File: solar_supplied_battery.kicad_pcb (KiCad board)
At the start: 2 copper layers, 16 parts, among them J1 Conn_01x02_Pin, J2 Conn_01x02_Pin, J3 Conn_01x02_Pin, J4 Conn_01x02_Pin, Q1 2N7002, U1 AP3015AKTR-G1

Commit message: starting routes
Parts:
- J1, J2: footprint Connector_PinHeader_2.54mm:PinHeader_1x02_P2.54mm_Vertical -> TerminalBlock:TerminalBlock_MaiXu_MX126-5.0-02P_1x02_P5.00mm
- J4: footprint Connector_PinHeader_2.54mm:PinHeader_1x02_P2.54mm_Horizontal -> TerminalBlock:TerminalBlock_MaiXu_MX126-5.0-02P_1x02_P5.00mm
- moved J1 90.3 mm to (105.1, 68.0), turned to 90 degrees
- moved R4 80.1 mm to (91.2, 61.2), turned to 180 degrees
- moved C2 79.5 mm to (99.0, 68.0), turned to 90 degrees
- moved C3 77.0 mm to (98.3, 61.2), turned to 180 degrees
- moved R3 75.3 mm to (87.6, 66.9)
- moved C1 72.0 mm to (90.3, 69.1), turned to 90 degrees
- moved R2 68.4 mm to (94.6, 65.4), turned to 180 degrees
- moved R1 65.3 mm to (98.4, 63.9), turned to 180 degrees
- moved Q1 55.3 mm to (91.2, 64.8), turned to -90 degrees
- moved U1 50.8 mm to (94.4, 69.2), turned to 180 degrees
- moved L1 47.4 mm to (89.8, 75.1), turned to 180 degrees
- moved J4 45.6 mm to (78.0, 62.0)
- moved J2 41.9 mm to (75.4, 73.1), turned to 180 degrees
- moved J3 38.5 mm to (82.3, 74.4), turned to 180 degrees
- moved D2 35.8 mm to (84.0, 65.5), turned to 90 degrees
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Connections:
- D1 pad A: /OUT_P -> Net-(U1-SW)
- L1 pad 1: /OUT_P -> Net-(U1-SW)
- U1 pad 1: /OUT_P -> Net-(U1-SW)

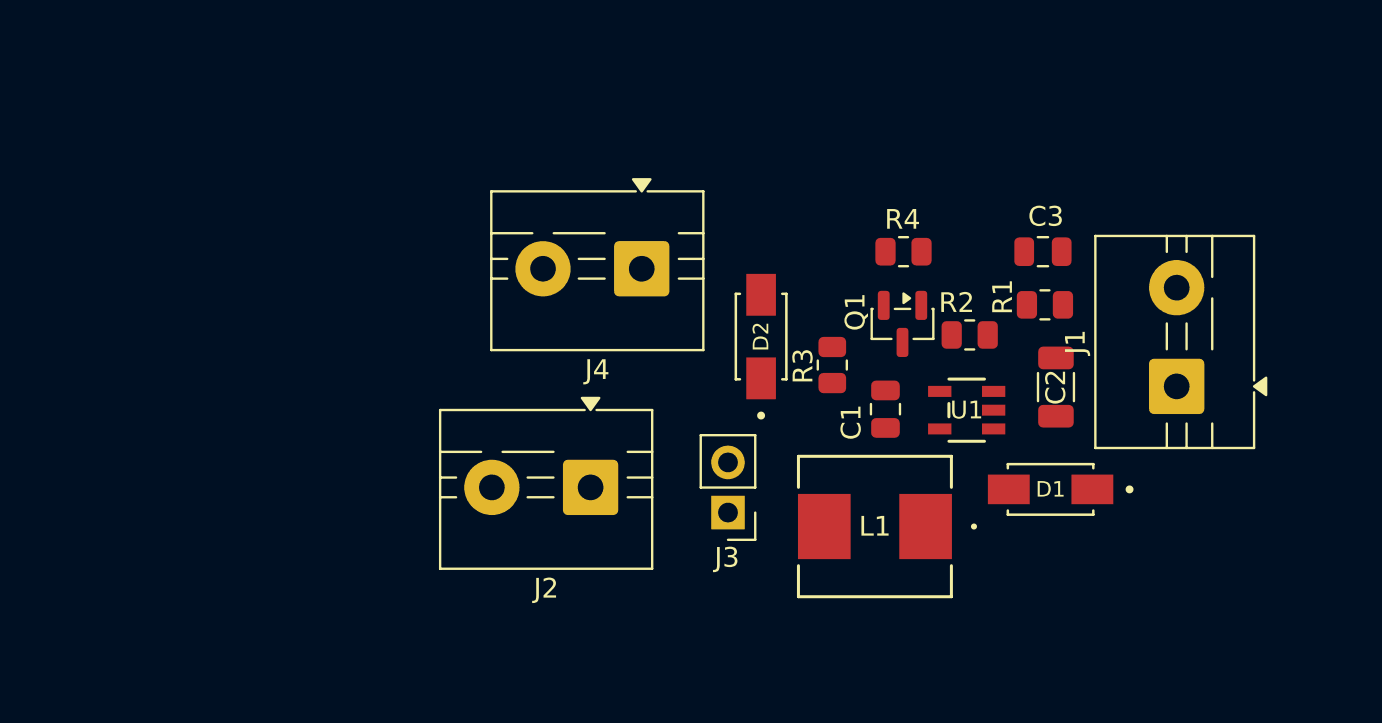
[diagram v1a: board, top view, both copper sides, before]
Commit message: reorganized folders and importing footprints
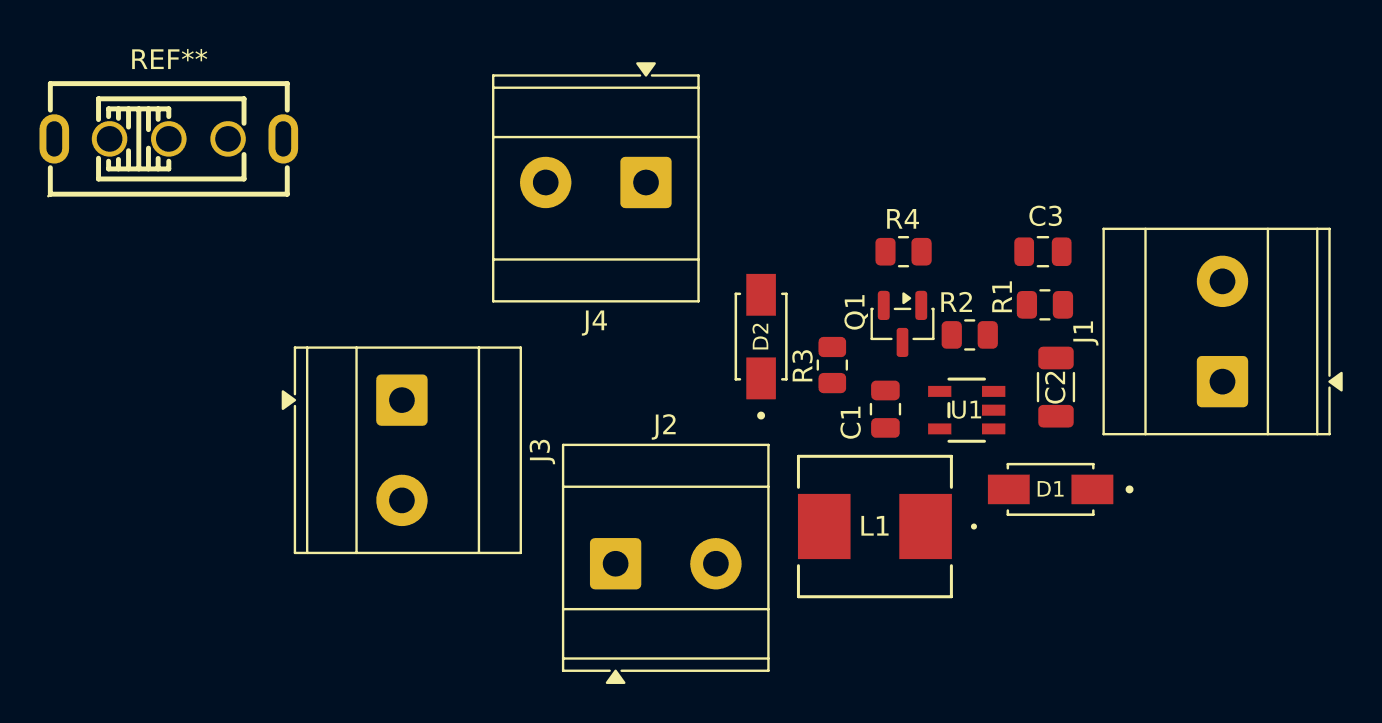
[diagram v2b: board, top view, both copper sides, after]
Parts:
- added REF**: SW-TH_SS-12F44-G5, jlcpcb:SW-TH_SS-12F44-G5, F.Cu at (54.0, 55.5)
- J1, J2, J4: footprint TerminalBlock:TerminalBlock_MaiXu_MX126-5.0-02P_1x02_P5.00mm -> TerminalBlock_Phoenix:TerminalBlock_Phoenix_MKDS-3-2-5.08_1x02_P5.08mm_Horizontal
- J3: footprint Connector_PinHeader_2.54mm:PinHeader_1x02_P2.54mm_Vertical -> TerminalBlock_Phoenix:TerminalBlock_Phoenix_MKDS-3-2-5.08_1x02_P5.08mm_Horizontal
- moved J3 17.5 mm to (65.8, 68.7), turned to -90 degrees
- moved J4 4.37 mm to (78.2, 57.7)
- moved J2 4.07 mm to (76.7, 77.0), turned to 0 degrees
- moved J1 2.33 mm to (107.4, 67.7)

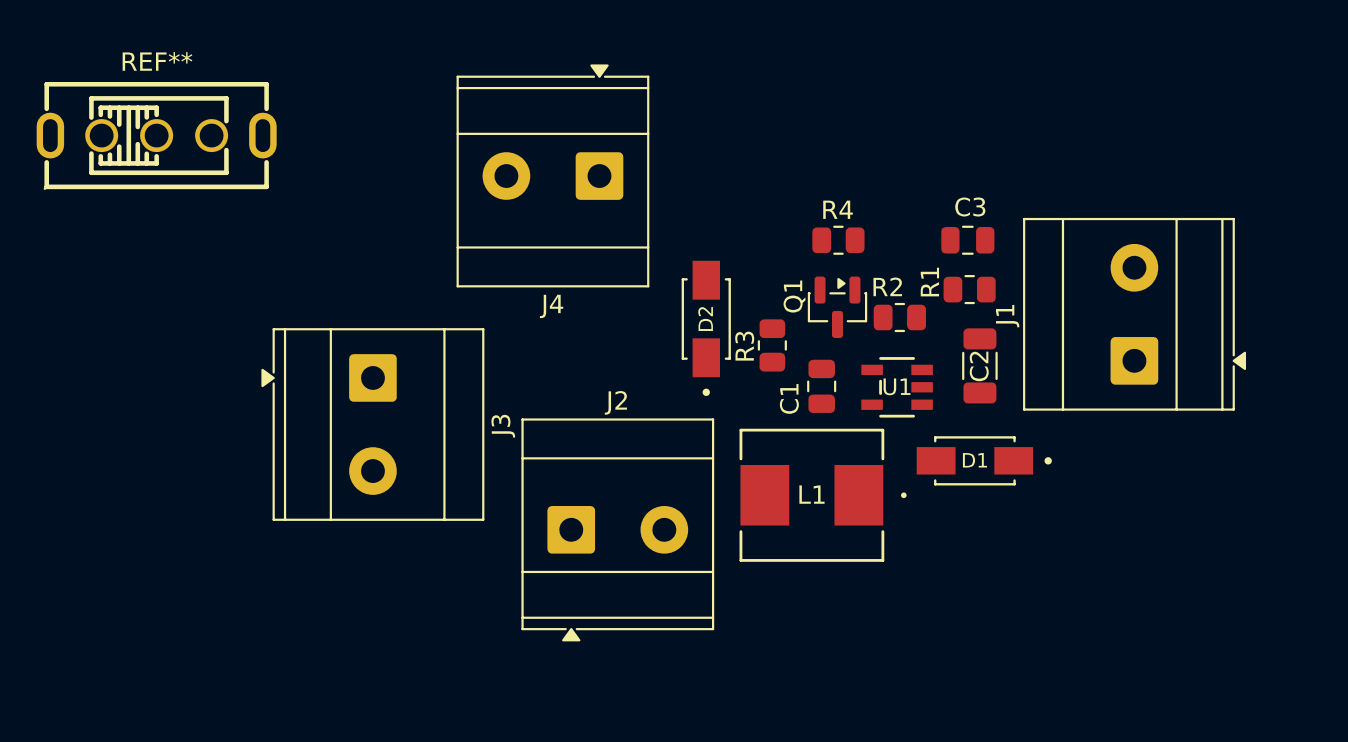
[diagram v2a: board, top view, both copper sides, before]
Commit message: finished routing, now just have to make vias for the ground fills
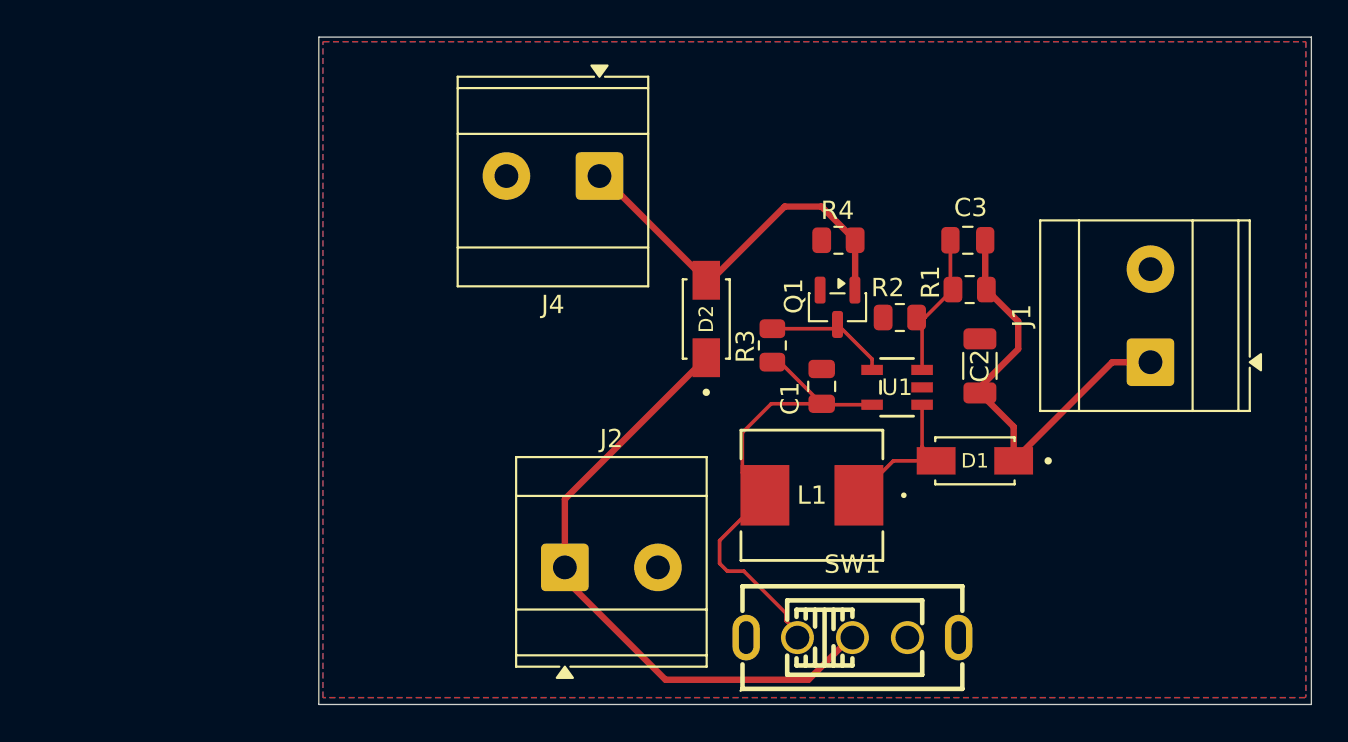
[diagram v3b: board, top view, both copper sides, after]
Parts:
- removed REF**: SW-TH_SS-12F44-G5, jlcpcb:SW-TH_SS-12F44-G5
- J1, J2, J4: value Conn_01x02_Pin -> WJ500V-5.08-2P
- SW1: renamed from J3; value Conn_01x02_Pin -> SS-12F44-G5; footprint TerminalBlock_Phoenix:TerminalBlock_Phoenix_MKDS-3-2-5.08_1x02_P5.08mm_Horizontal -> jlcpcb:SW-TH_SS-12F44-G5
- moved SW1 29.8 mm to (92.0, 82.8), turned to 0 degrees
- moved J2 2.08 mm to (76.3, 79.0)
- moved J1 0.88 mm to (108.3, 67.8)
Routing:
- net /BAT_P: track 0.00 -> 34.2 mm
- net Net-(SW1-A): track 0.00 -> 26.4 mm
- net /OUT_P: track 0.00 -> 24.1 mm
- net /SOLAR_P: track 0.00 -> 21.5 mm
- net Net-(U1-SW): track 0.00 -> 8.38 mm
- net Net-(U1-FB): track 0.00 -> 8.35 mm
- net Net-(Q1-D): track 0.00 -> 6.91 mm
- added copper zone on B.Cu, net GNDD
- added copper zone on F.Cu, net GNDD
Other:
- board outline added: 54.2 x 36.4 mm

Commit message: finalized the physical components, just have to do gerber and bom
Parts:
- added G***: LOGO, logos:muffinByteLogo, F.Cu at (110.2, 76.5)
- L1: footprint ul_ASPI-0630LR-100M-T15:IND_ASPI-0630LR_ABR -> ASPI-0630LR-100M-T15:IND_ASPI-0630LR-100M-T15
- moved R2 1.40 mm to (95.8, 66.1)
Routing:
- net GNDD: vias 0 -> 14
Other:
- board text added: "+"
- board text added: "-"
- board text added: "BAT"
- board text added: "MuffinByteLabs.com"
- board text added: "ON/OFF"
- board text added: "OUT"
- board text added: "Ray Malik"
- board text added: "SOLAR"

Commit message: finished layout and bom
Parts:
- C1: value 4.7 uF, 50 V, X7R (0805) -> 4.7 µF, 25 V, X5R (0805)
- C2: value 22 uF, 10 V X7R (1206) -> 22 µF, 25 V, X5R (1206)
- C3: value 10 pF, 50 V, X7R (0805) -> 10 pF, 50 V, C0G (0805)
- D1, D2: footprint SS14:DIOM4325X250N -> SS14:SS14
- SW1: footprint jlcpcb:SW-TH_SS-12F44-G5 -> SW-TH_SS-12F44-G5:SW-TH_SS-12F44-G5
- U1: footprint ul_AP3015AKTR-G1:SOT23-5_1P55X2P9_DIO -> AP3015AKTR-G1:AP3015AKTR-G1
- moved G*** 0.20 mm to (110.2, 76.2)
